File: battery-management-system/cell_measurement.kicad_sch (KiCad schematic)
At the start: 23 parts

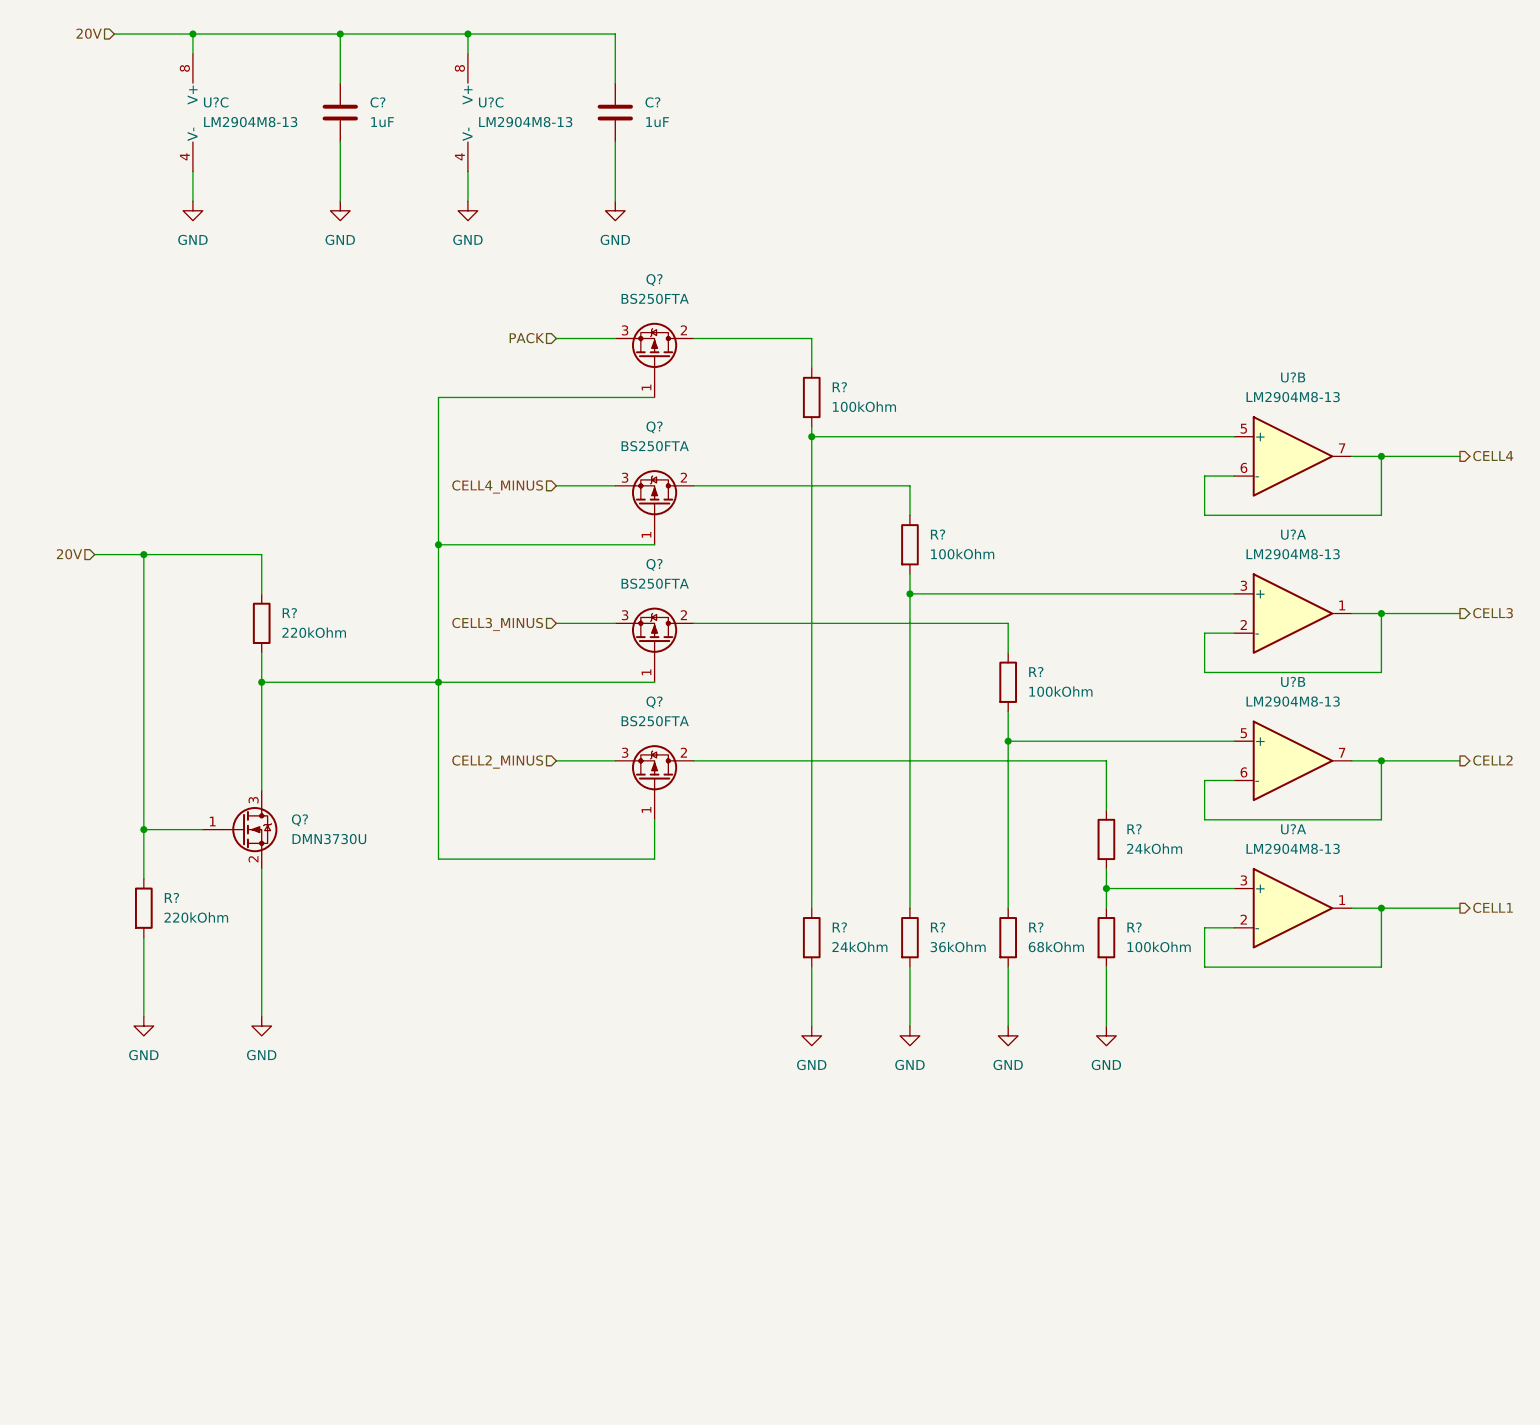
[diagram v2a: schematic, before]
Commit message: route UART and ADC channels on MCU
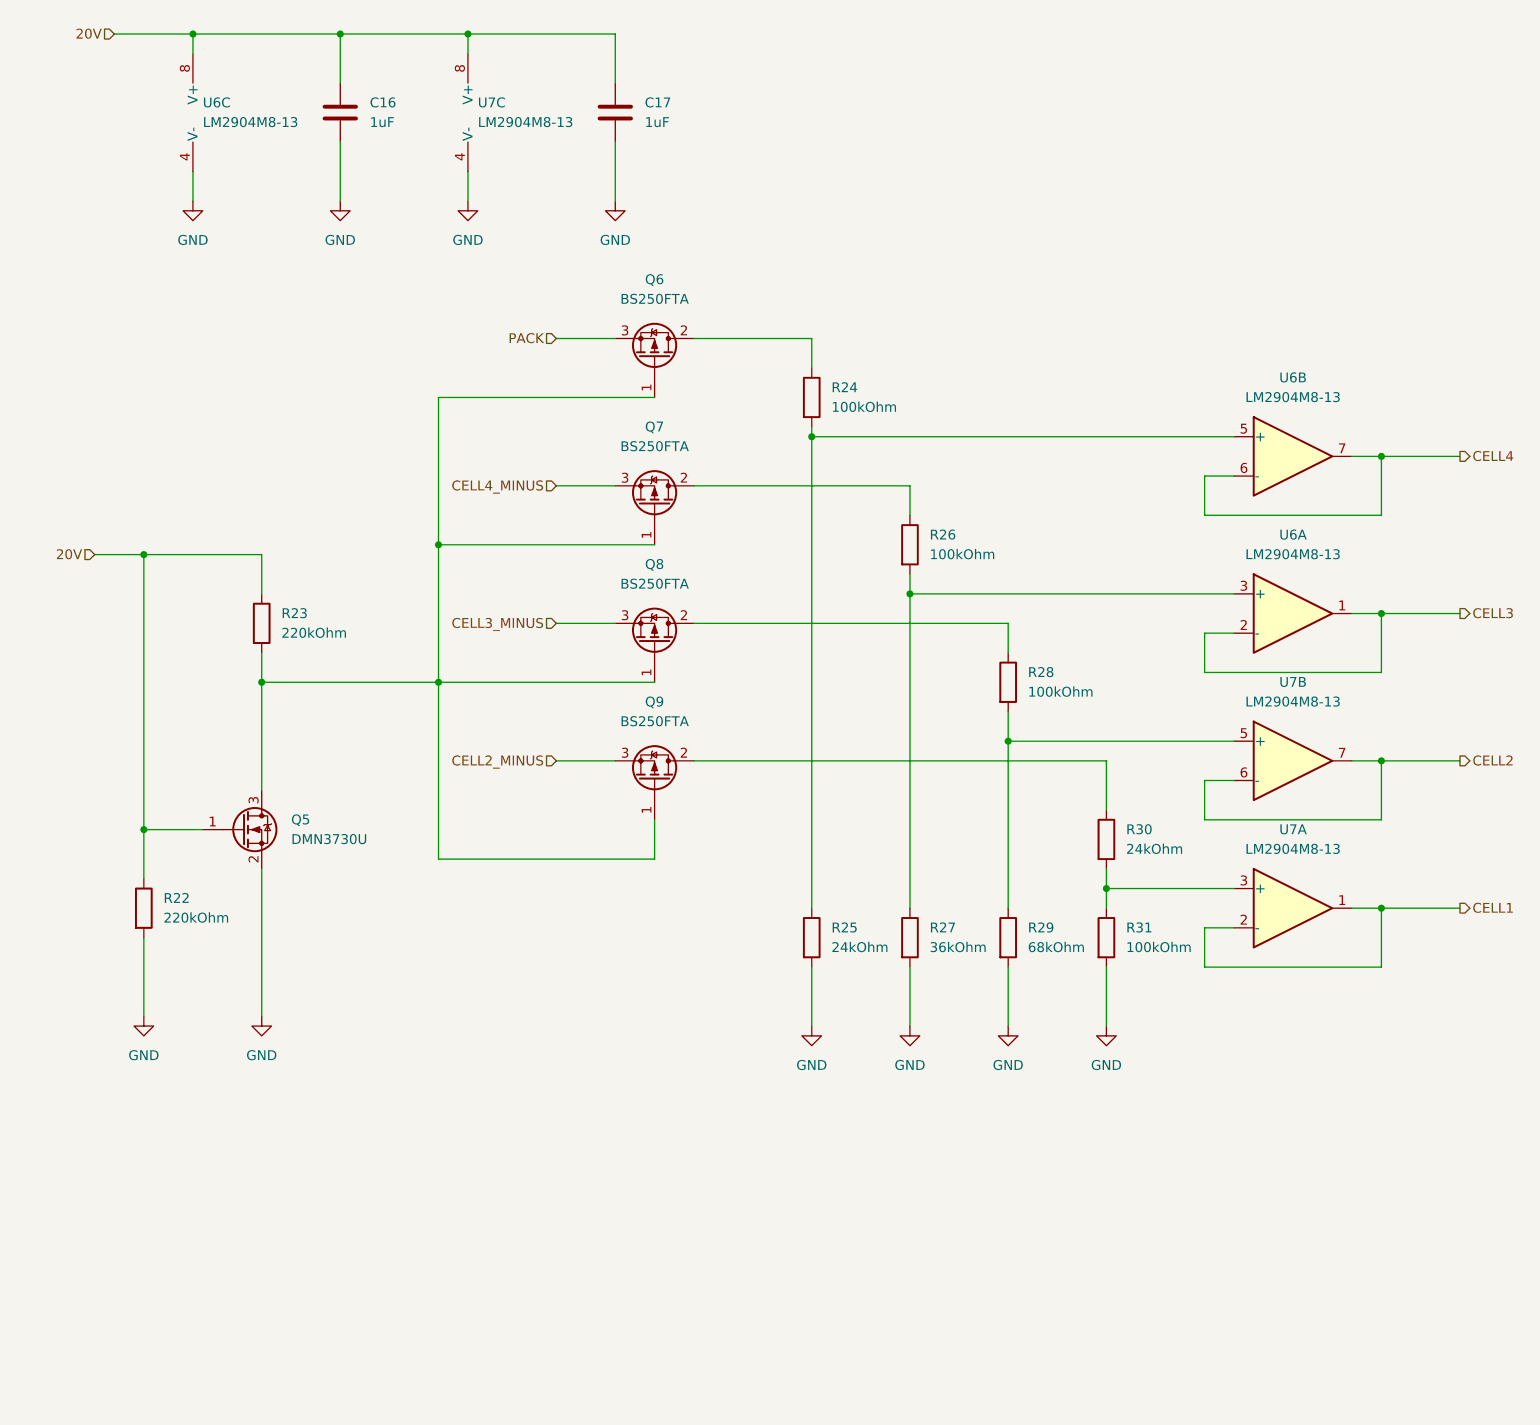
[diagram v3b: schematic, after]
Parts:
- gave numbers to parts that had none: 19

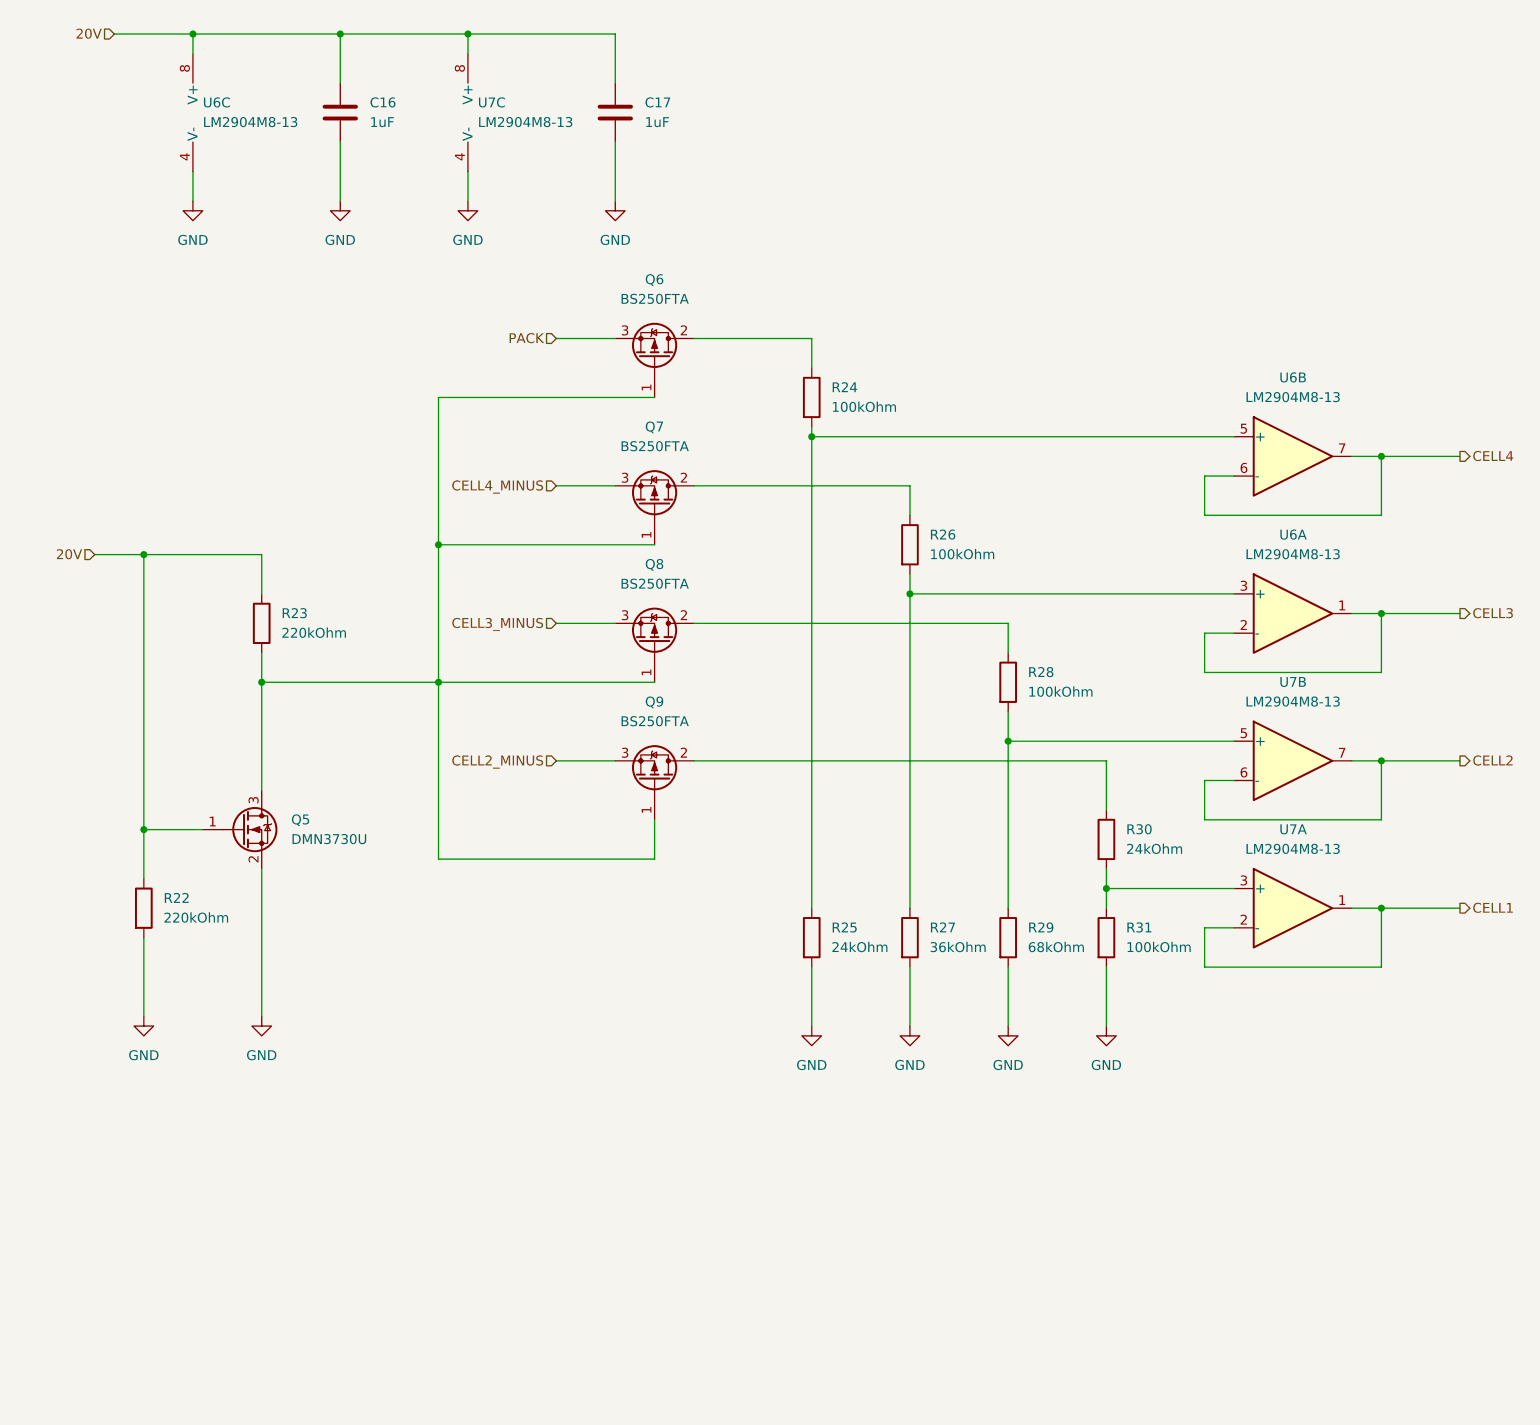
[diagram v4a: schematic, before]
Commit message: improve usage of net labels
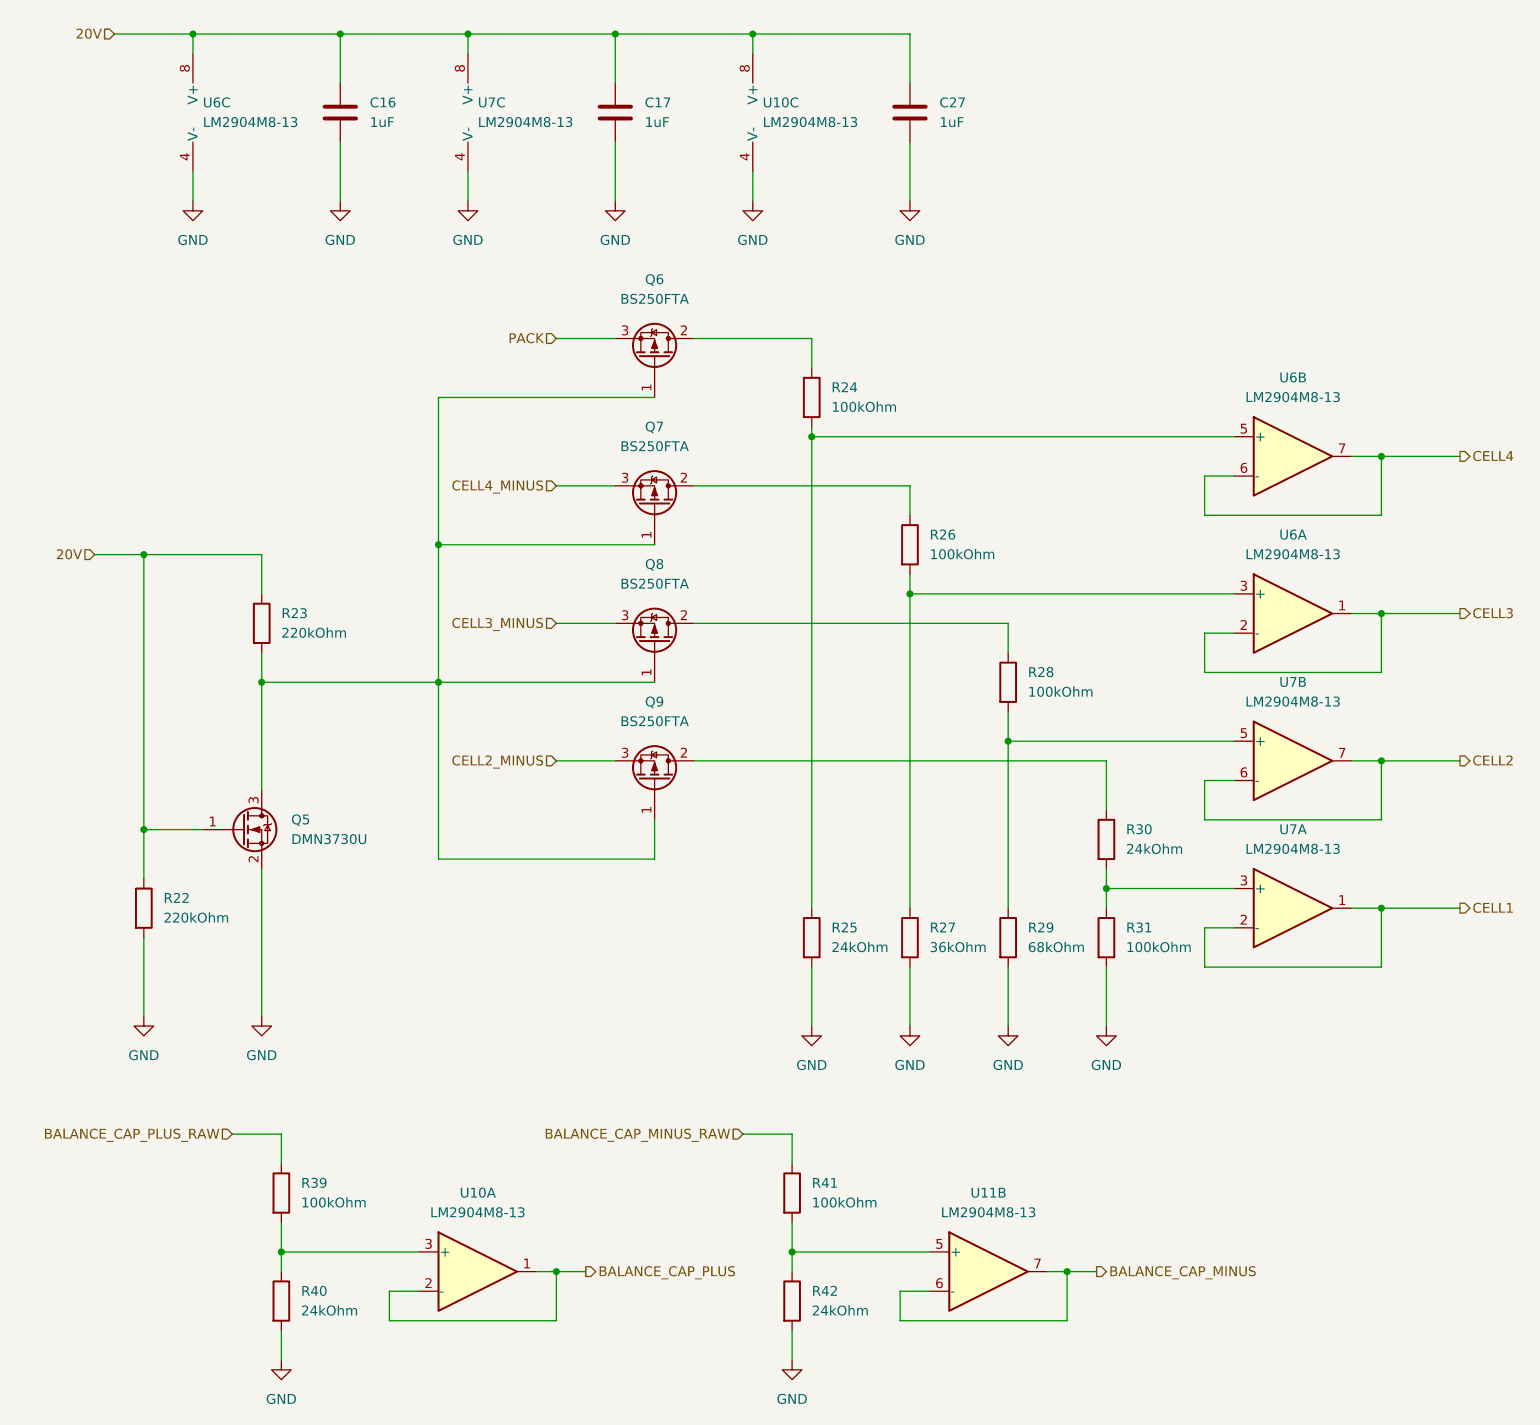
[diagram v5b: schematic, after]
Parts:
- added C27: 1uF, benediktibk:C_0603_1608Metric_Pad1.08x0.95mm_HandSolder, symbol benediktibk:C_1uF_SMD_0603_50V_10%
- added R39, R41: 100kOhm, benediktibk:R_0603_1608Metric_Pad0.98x0.95mm_HandSolder, symbol benediktibk:R_100kOhm_SMD_0603_100mW_1%
- added R40, R42: 24kOhm, benediktibk:R_0603_1608Metric_Pad0.98x0.95mm_HandSolder, symbol benediktibk:R_24kOhm_SMD_0603_100mW_1%
- added U10, U11: LM2904M8-13, benediktibk:MSOP-8_3x3mm_P0.65mm, symbol benediktibk:LM2904M8-13
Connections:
- net 20V: now also C27.1, U10.8 (V+)
- net GND: now also C27.2, R40.2, R42.2, U10.4 (V-)
- new net: R39.2, R40.1, U10.3 (+)
- new net: R41.2, R42.1, U11.5 (+)
- new net BALANCE_CAP_MINUS: U11.6 (-), U11.7
- new net BALANCE_CAP_MINUS_RAW: R41.1
- new net BALANCE_CAP_PLUS: U10.1, U10.2 (-)
- new net BALANCE_CAP_PLUS_RAW: R39.1

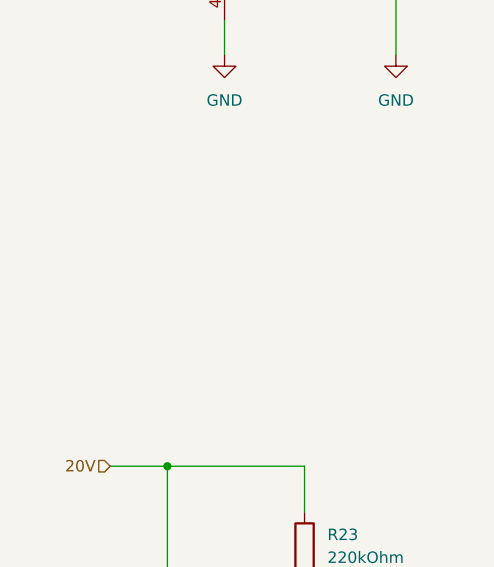
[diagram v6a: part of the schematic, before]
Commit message: add balancing sheet
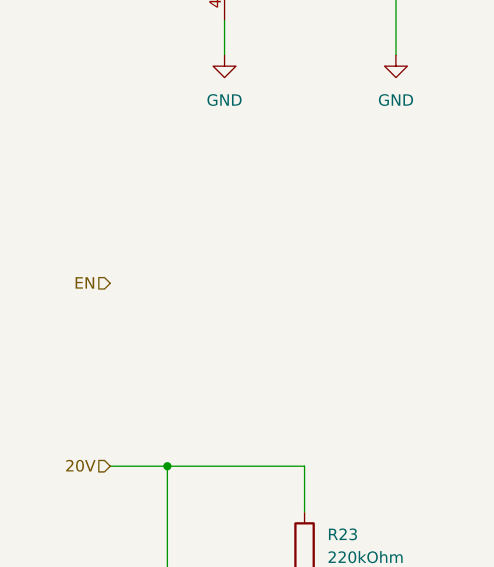
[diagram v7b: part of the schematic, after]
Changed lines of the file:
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@@
     (effects (font (size 1.27 1.27)) (justify left))
+  )
+  (hierarchical_label "EN" (shape input) (at 22.86 62.23 180) (fields_autoplaced)
+    (effects (font (size 1.27 1.27)) (justify right))
   )
   (hierarchical_label "CELL3" (shape output) (at 199.39 90.17 0) (fields_autoplaced)
